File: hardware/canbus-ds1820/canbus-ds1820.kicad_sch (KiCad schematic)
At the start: 33 parts, among them J1 USB_B_Micro, J2 UART, J3 10k NTC, J4 CANBus, J5 CANBus, J6 SWD, Q1 2N7002, Q2 2N7002, U1 MCP1754S-3302xCB, U2 STM32F042F6Px, U3 Voltage Regulator, U4 MCP2562HD

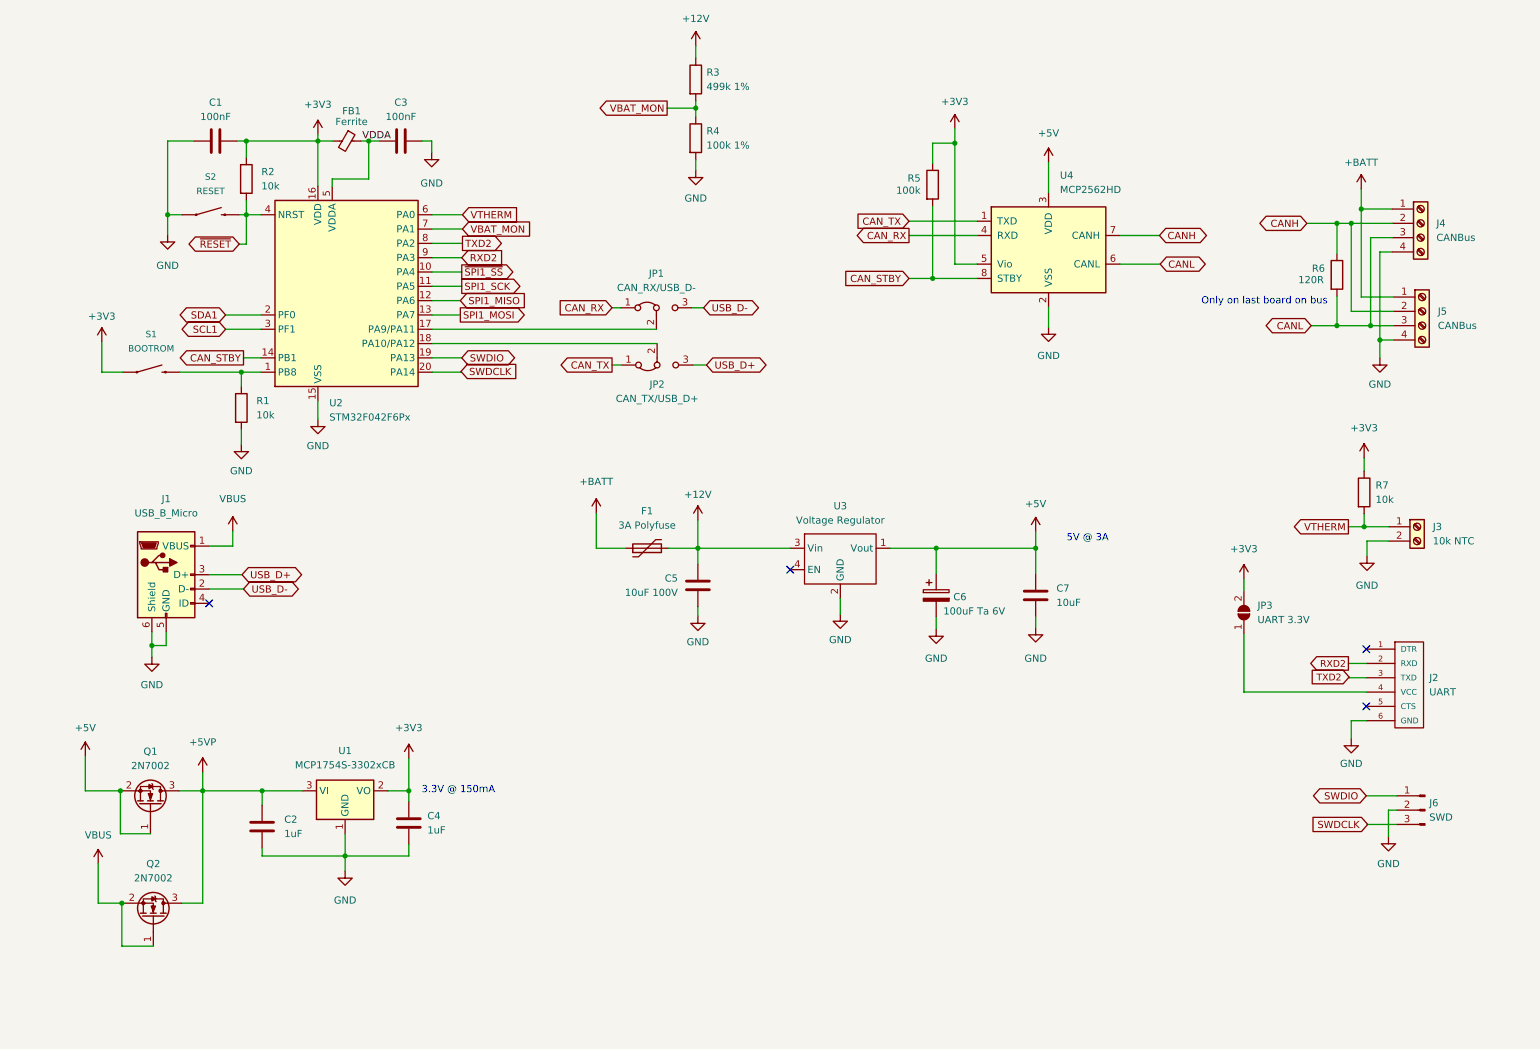
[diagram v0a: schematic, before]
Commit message: Updated canbus-ds1820 board, reannotated canbus-gpios
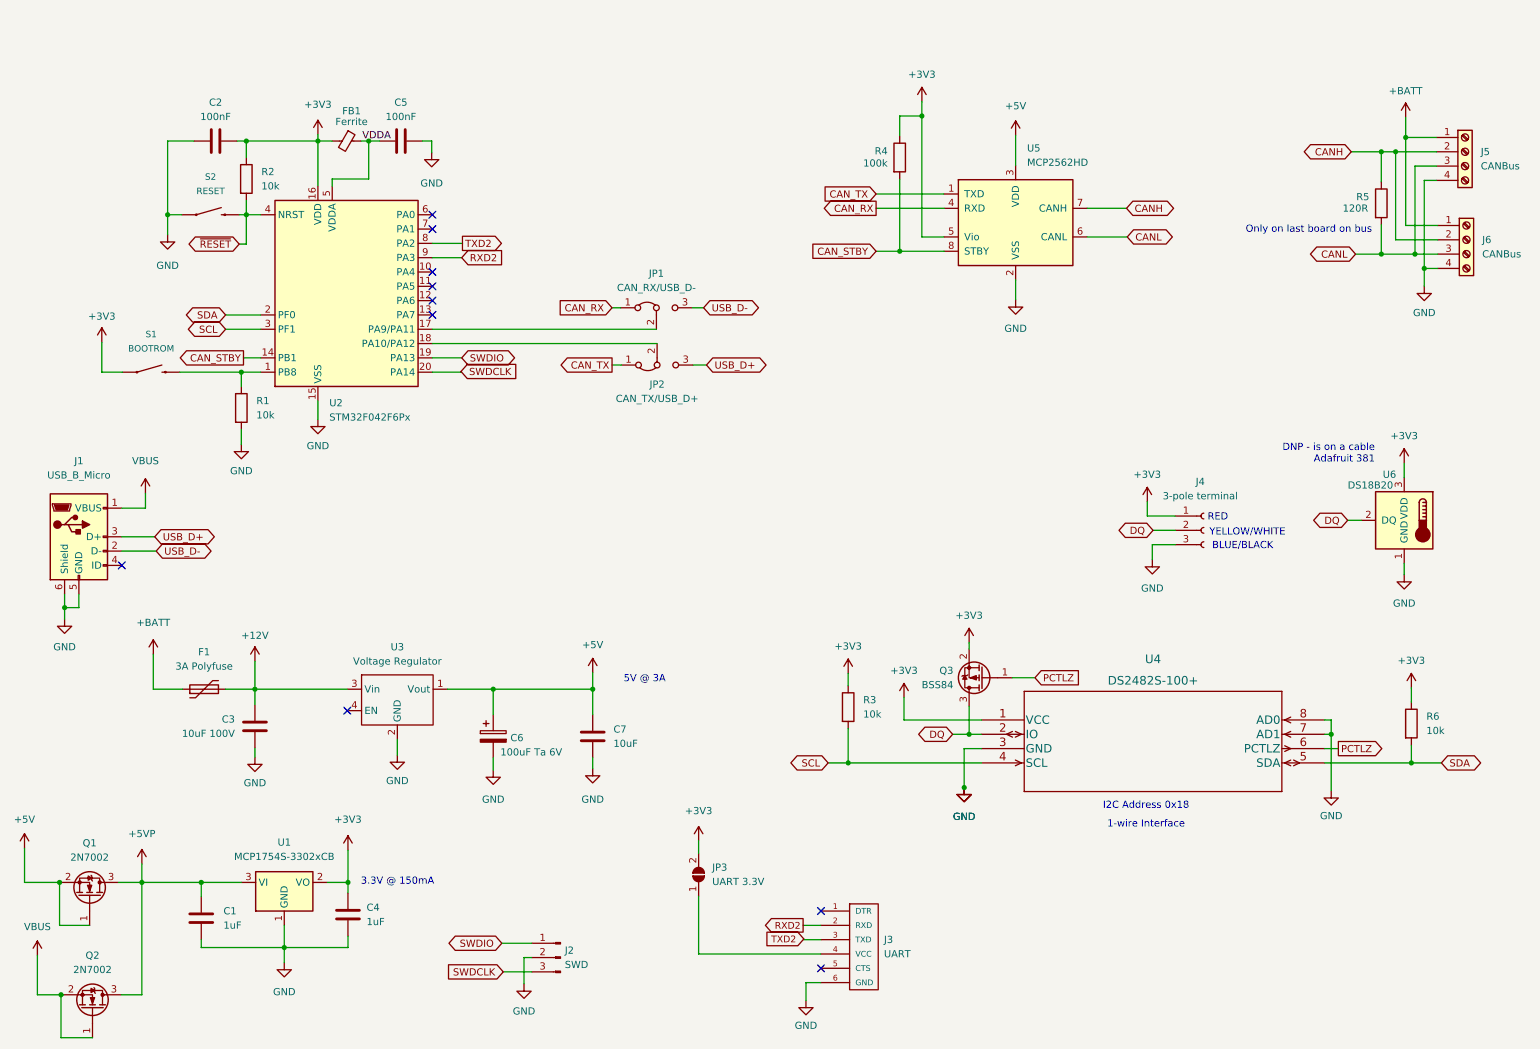
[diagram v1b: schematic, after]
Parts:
- removed J3: 10k NTC, TerminalBlock_TE-Connectivity:TerminalBlock_TE_282834-2_1x02_P2.54mm_Horizontal, symbol Connector:Screw_Terminal_01x02
- removed R4: 100k 1%, Resistor_SMD:R_0805_2012Metric_Pad1.20x1.40mm_HandSolder, symbol Device:R
- removed R7: 10k, Resistor_SMD:R_0805_2012Metric_Pad1.20x1.40mm_HandSolder, symbol Device:R
- added J4: 3-pole terminal, TerminalBlock_TE-Connectivity:TerminalBlock_TE_282834-3_1x03_P2.54mm_Horizontal, symbol Connector:Conn_01x03_Female
- added Q3: BSS84, Package_TO_SOT_SMD:SOT-23, symbol Transistor_FET:BSS84
- added R6: 10k, Resistor_SMD:R_0805_2012Metric_Pad1.20x1.40mm_HandSolder, symbol Device:R
- added U4: DS2482S-100+, UltraLibrarian:DS2482S-100&plus_, symbol UltraLibrarian:DS2482S-100+
- added U6: DS18B20, Package_TO_SOT_THT:TO-92_Inline, symbol Sensor_Temperature:DS18B20
- JP3: footprint (none) -> Jumper:SolderJumper-2_P1.3mm_Open_TrianglePad1.0x1.5mm
- R3: value 499k 1% -> 10k
- renumbered C2 to C1, C1 to C2, C5 to C3, C3 to C5, J6 to J2, J2 to J3, J4 to J5, J5 to J6, R5 to R4, R6 to R5, U4 to U5
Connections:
- net +12V: no longer R3.1
- net +3V3: now also R3.1, J4.1 (Pin_1), Q3.2 (S), R6.1, U4.1 (VCC), U6.3 (VDD)
- net GND: now also J4.3 (Pin_3), U4.3 (GND), U4.7 (AD1), U4.8 (AD0), U6.1 (GND)
- net SCL1 renamed SCL
- net SCL: now also R3.2, U4.4 (SCL)
- net SDA1 renamed SDA
- net SDA: now also R6.2, U4.5 (SDA)
- net SPI1_MISO: no longer names the net of U2.12 (PA6)
- net SPI1_MOSI: no longer names the net of U2.13 (PA7)
- net SPI1_SCK: no longer names the net of U2.11 (PA5)
- net VBAT_MON: no longer names the net of U2.7 (PA1)
- net VBAT_MON: no longer R3.2
- net VTHERM: no longer names the net of U2.6 (PA0)
- net ~{SPI1_SS}: no longer names the net of U2.10 (PA4)
- new net DQ: J4.2 (Pin_2), Q3.3 (D), U4.2 (IO), U6.2 (DQ)
- new net PCTLZ: Q3.1 (G), U4.6 (PCTLZ)
- no-connect marks 4 -> 10
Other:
- note added: "1-wire Interface"
- note added: "BLUE/BLACK"
- note added: "DNP - is on a cable Adafruit 381"
- note added: "I2C Address 0x18"
- note added: "RED"
- note added: "YELLOW/WHITE"
- title: CANBus Thermistor Sensor -> CANBus DS1820 Sensor
- moved on the sheet: C1, C3, C4, C6, C7, F1, J1, J2, J3, J5, J6, JP3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
